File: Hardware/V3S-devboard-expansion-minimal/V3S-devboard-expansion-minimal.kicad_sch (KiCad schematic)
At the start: 2 parts, among them CN1 AS0BC21-S30BE-7H, CN2 AS0BC21-S30BE-7H

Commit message: expansion board work
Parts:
- added C1, C2: 100n, Capacitor_SMD:C_0603_1608Metric, symbol Device:C_Small
- added C10, C3, C5, C7, C8, C9: 10u, Capacitor_SMD:C_0603_1608Metric, symbol Device:C_Small
- added C4, C6: 1u, Capacitor_SMD:C_0603_1608Metric, symbol Device:C_Small
- added FPC1: AFC07-S50ECA-00, v3s-devboard-expansion-minimal:FPC-SMD_AFC07-S50ECA-00, symbol v3s-devboard-expansion-minimal:AFC07-S50ECA-00
- added J1, J2, J3: Conn_01x05_Pin, Connector_PinHeader_2.54mm:PinHeader_1x05_P2.54mm_Vertical, symbol Connector:Conn_01x05_Pin
- added J10: USB_C_Receptacle_USB2.0, Connector_USB:USB_C_Receptacle_HCTL_HC-TYPE-C-16P-01A, symbol Connector:USB_C_Receptacle_USB2.0
- added J11, J12, J4, J6: Conn_01x02_Pin, Connector_PinHeader_2.54mm:PinHeader_1x02_P2.54mm_Vertical, symbol Connector:Conn_01x02_Pin
- added J13: Conn_01x03_Pin, Connector_PinSocket_2.54mm:PinSocket_1x03_P2.54mm_Vertical, symbol Connector:Conn_01x03_Pin
- added J5: Conn_02x05_Odd_Even, Connector_PinHeader_2.54mm:PinHeader_2x05_P2.54mm_Vertical, symbol Connector_Generic:Conn_02x05_Odd_Even
- added J7: Conn_02x12_Odd_Even, Connector_PinSocket_2.54mm:PinSocket_2x12_P2.54mm_Vertical, symbol Connector_Generic:Conn_02x12_Odd_Even
- added J8: RJ45_Hanrun_HR911105A_Horizontal, Connector_RJ:RJ45_Hanrun_HR911105A_Horizontal, symbol Connector:RJ45_Hanrun_HR911105A_Horizontal
- added J9: Conn_02x03_Odd_Even, Connector_PinSocket_2.54mm:PinSocket_2x03_P2.54mm_Vertical, symbol Connector_Generic:Conn_02x03_Odd_Even
- added L1: 2.2u, Inductor_SMD:L_1008_2520Metric, symbol Device:L_Small
- added R1, R2, R3, R4: 100, Resistor_SMD:R_0603_1608Metric, symbol Device:R_Small_US
- added R10, R11, R8, R9: 51, Resistor_SMD:R_0603_1608Metric, symbol Device:R_Small_US
- added R12, R14: 5.1K, Resistor_SMD:R_0603_1608Metric, symbol Device:R_Small_US
- added R13: 4.7K, Resistor_SMD:R_0603_1608Metric, symbol Device:R_Small_US
- added R5, R7: 680, Resistor_SMD:R_0603_1608Metric, symbol Device:R_Small_US
- added R6: 10k, Resistor_SMD:R_0402_1005Metric, symbol Device:R_Small_US
- added U1: CP2102N-Axx-xQFN28, Package_DFN_QFN:QFN-28-1EP_5x5mm_P0.5mm_EP3.1x3.1mm, symbol Interface_USB:CP2102N-Axx-xQFN28
- added U2: XDFC-0522-50P, v3s-devboard-expansion-minimal:FPC-SMD_50P-P0.50_LX_XDFC-0522-50P, symbol v3s-devboard-expansion-minimal:XDFC-0522-50P
- added U3: AMS1117-3.3, Package_TO_SOT_SMD:SOT-223-3_TabPin2, symbol Regulator_Linear:AMS1117-3.3
- added U4: AMS1117-2.85, Package_TO_SOT_SMD:SOT-223-3_TabPin2, symbol Regulator_Linear:AMS1117-2.85
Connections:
- net 5V: now also J11.2 (Pin_2)
- net CSI.CSI_SCK: now also J7.9 (Pin_9)
- net CSI.CSI_SDA: now also J7.8 (Pin_8)
- net CSI.MCSI_CK_N: now also J7.2 (Pin_2)
- net CSI.MCSI_CK_P: now also J7.4 (Pin_4)
- net CSI.MCSI_D0_N: now also J7.5 (Pin_5)
- net CSI.MCSI_D0_P: now also J7.7 (Pin_7)
- net CSI.MCSI_D1_N: now also J7.1 (Pin_1)
- net CSI.MCSI_D1_P: now also J7.3 (Pin_3)
- net CSI.MCSI_MCLK: now also J7.6 (Pin_6)
- net ETH0.RX_N: now also J8.6 (RD-), R11.2
- net ETH0.RX_P: now also J8.3 (RD+), R10.2
- net ETH0.TX_N: now also J8.2 (TD-), R9.2
- net ETH0.TX_P: now also J8.1 (TD+), R8.2
- net ETH_LED_LINK: now also J8.10
- net ETH_LED_SPD: now also J8.11
- net GND: now also CN1.76, CN1.77, C1.1, C10.1, C2.1, C3.1, C4.1, C5.1, C6.1, C7.1, C8.1, C9.1, FPC1.43, FPC1.48, FPC1.49, FPC1.50, FPC1.51, FPC1.52, J10.A1 (GND), J10.A12 (GND), J10.B1 (GND), J10.B12 (GND), J10.S1 (SHIELD), J2.1 (Pin_1), J2.2 (Pin_2), J2.3 (Pin_3), J2.4 (Pin_4), J2.5 (Pin_5), J5.9 (Pin_9), J7.20 (Pin_20), J7.22 (Pin_22), J7.24 (Pin_24), J8.8, J8.SH, J9.5 (Pin_5), J9.6 (Pin_6), R1.2, R12.2, R14.2, R2.2, R3.2, R4.2, U1.29 (GND), U1.3 (GND), U2.43, U2.48, U2.49, U2.50, U2.51, U2.52, U3.1 (GND), U4.1 (GND)
- net LCD0.CLK: now also FPC1.13, U2.13
- net LCD0.DE: now also J6.1 (Pin_1)
- net LCD0.HSYNC: now also FPC1.12, U2.12
- net LCD0.VSYNC: now also FPC1.11, U2.11
- net LCD_D10: now also FPC1.26, U2.26
- net LCD_D11: now also FPC1.25, U2.25
- net LCD_D12: now also FPC1.24, U2.24
- net LCD_D13: now also FPC1.23, U2.23
- net LCD_D14: now also FPC1.22, U2.22
- net LCD_D15: now also FPC1.21, U2.21
- net LCD_D18: now also FPC1.20, U2.20
- net LCD_D19: now also FPC1.19, U2.19
- net LCD_D2: now also FPC1.32, U2.32
- net LCD_D20: now also FPC1.18, U2.18
- net LCD_D21: now also FPC1.17, U2.17
- net LCD_D22: now also FPC1.16, U2.16
- net LCD_D23: now also FPC1.15, U2.15
- net LCD_D3: now also FPC1.31, U2.31
- net LCD_D4: now also FPC1.30, U2.30
- net LCD_D5: now also FPC1.29, U2.29
- net LCD_D6: now also FPC1.28, U2.28
- net LCD_D7: now also FPC1.27, U2.27
- net PB4_PWM0: now also J7.16 (Pin_16)
- net PB5_PWM1: now also J7.15 (Pin_15)
- net PB6_SCK: now also J7.13 (Pin_13)
- net PB7_SDA: now also J7.14 (Pin_14)
- net SDC1.CLK: now also J7.10 (Pin_10)
- net SDC1.D0: now also J7.12 (Pin_12)
- net SDC1.D2: now also J7.11 (Pin_11)
- net UART0.RX: now also J9.1 (Pin_1)
- net UART0.TX: now also J9.2 (Pin_2)
- net UART2.CTS: now also J7.17 (Pin_17)
- net UART2.RX: now also J9.3 (Pin_3)
- net UART2.TX: now also J9.4 (Pin_4)
- net USB.USB_ID: now also J7.18 (Pin_18)
- new net: C1.2, J8.5 (RCT), R10.1, R11.1
- new net: C2.2, J8.4 (TCT), L1.2, R8.1, R9.1
- new net: FPC1.44, U2.44
- new net: FPC1.45, U2.45
- new net: FPC1.46, U2.46
- new net: FPC1.47, U2.47
- new net: J8.9, R7.1
- new net: J10.B5 (CC2), R14.1
- new net: J8.12, R5.1
- new net: R13.1, U1.9 (~{RST})
- new net: J10.A5 (CC1), R12.1
- new net: J12.1 (Pin_1), U1.25 (RXD)
- new net: J12.2 (Pin_2), U1.26 (TXD)
- new net 2V85: C7.2, J13.1 (Pin_1), U4.2 (VO)
- new net 3V3: C5.2, C6.2, C8.2, J13.3 (Pin_3), J7.19 (Pin_19), J7.21 (Pin_21), J7.23 (Pin_23), L1.1, R13.2, R5.2, R7.2, U1.6 (VDD), U1.7 (VREGIN), U3.2 (VO)
- new net IM0: FPC1.6, J1.1 (Pin_1), U2.6
- new net IM1: FPC1.7, J1.2 (Pin_2), U2.7
- new net IM2: FPC1.8, J1.3 (Pin_3), U2.8
- new net IM3: FPC1.9, J1.4 (Pin_4), U2.9
- new net LCD_CS: FPC1.38, J5.7 (Pin_7), U2.38
- new net LCD_DE: FPC1.14, J6.2 (Pin_2), U2.14
- new net LCD_DRX: FPC1.36, J5.4 (Pin_4), U2.36
- new net LCD_RD: FPC1.35, J5.2 (Pin_2), U2.35
- new net LCD_RST: FPC1.10, J1.5 (Pin_5), R6.2, U2.10
- new net LCD_SCL: FPC1.37, J5.5 (Pin_5), U2.37
- new net LCD_SDI: FPC1.34, J5.3 (Pin_3), U2.34
- new net LCD_SDO: FPC1.33, J5.1 (Pin_1), U2.33
- new net LCD_TE: FPC1.39, J5.6 (Pin_6), U2.39
- new net LCD_VDD: FPC1.40, FPC1.41, FPC1.42, U2.40, U2.41, U2.42
- new net LEDA: FPC1.1, J4.2 (Pin_2), U2.1
- new net LEDK1: FPC1.2, R1.1, U2.2
- new net LEDK2: FPC1.3, R2.1, U2.3
- new net LEDK3: FPC1.4, R3.1, U2.4
- new net LEDK4: FPC1.5, R4.1, U2.5
- new net LED_VDD: J13.2 (Pin_2), J3.1 (Pin_1), J3.2 (Pin_2), J3.3 (Pin_3), J3.4 (Pin_4), J3.5 (Pin_5), J4.1 (Pin_1), R6.1
- new net USB_D_N: J10.A7 (D-), J10.B7 (D-), U1.5 (D-)
- new net USB_D_P: J10.A6 (D+), J10.B6 (D+), U1.4 (D+)
- new net VBUS_IN: C10.2, C3.2, C4.2, C9.2, J10.A4 (VBUS), J10.A9 (VBUS), J10.B4 (VBUS), J10.B9 (VBUS), J11.1 (Pin_1), U1.8 (VBUS), U3.3 (VI), U4.3 (VI)
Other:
- note added: "red 23-18 green 15-10 blue 2-7"
- note added: "top: C262650 bottom: C262574 clam both: C7527533"
- moved on the sheet: CN1, CN2

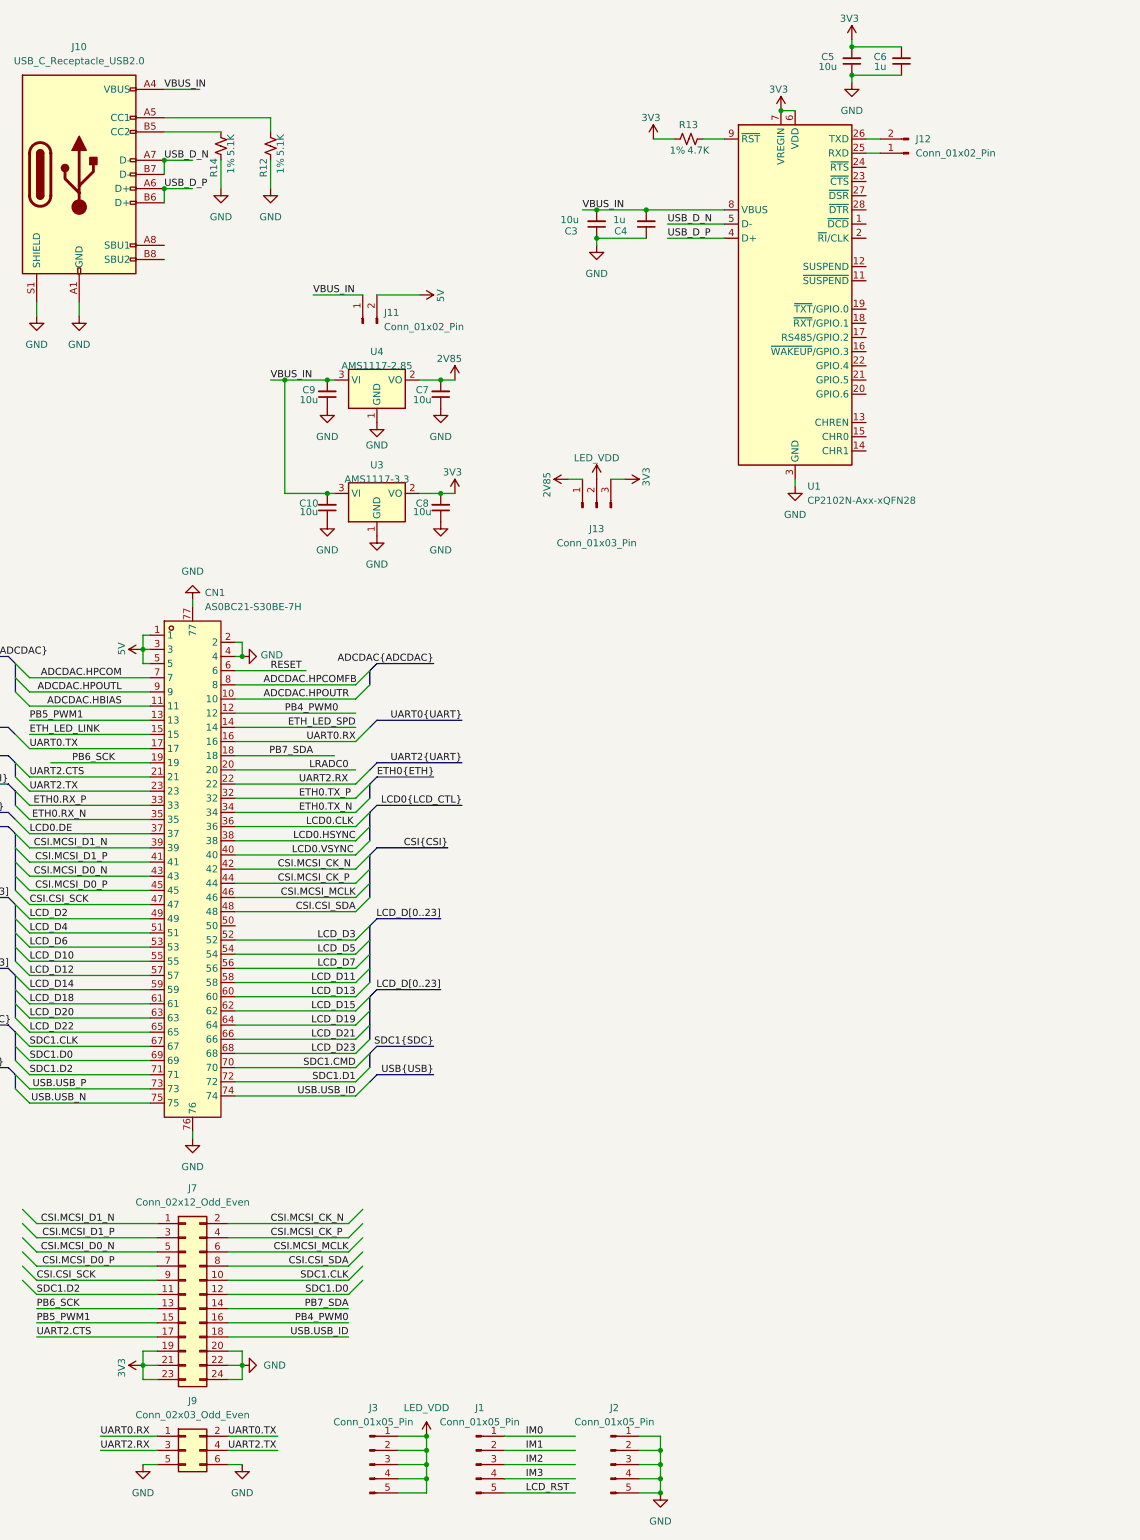
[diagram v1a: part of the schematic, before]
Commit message: expansion layout and schematic
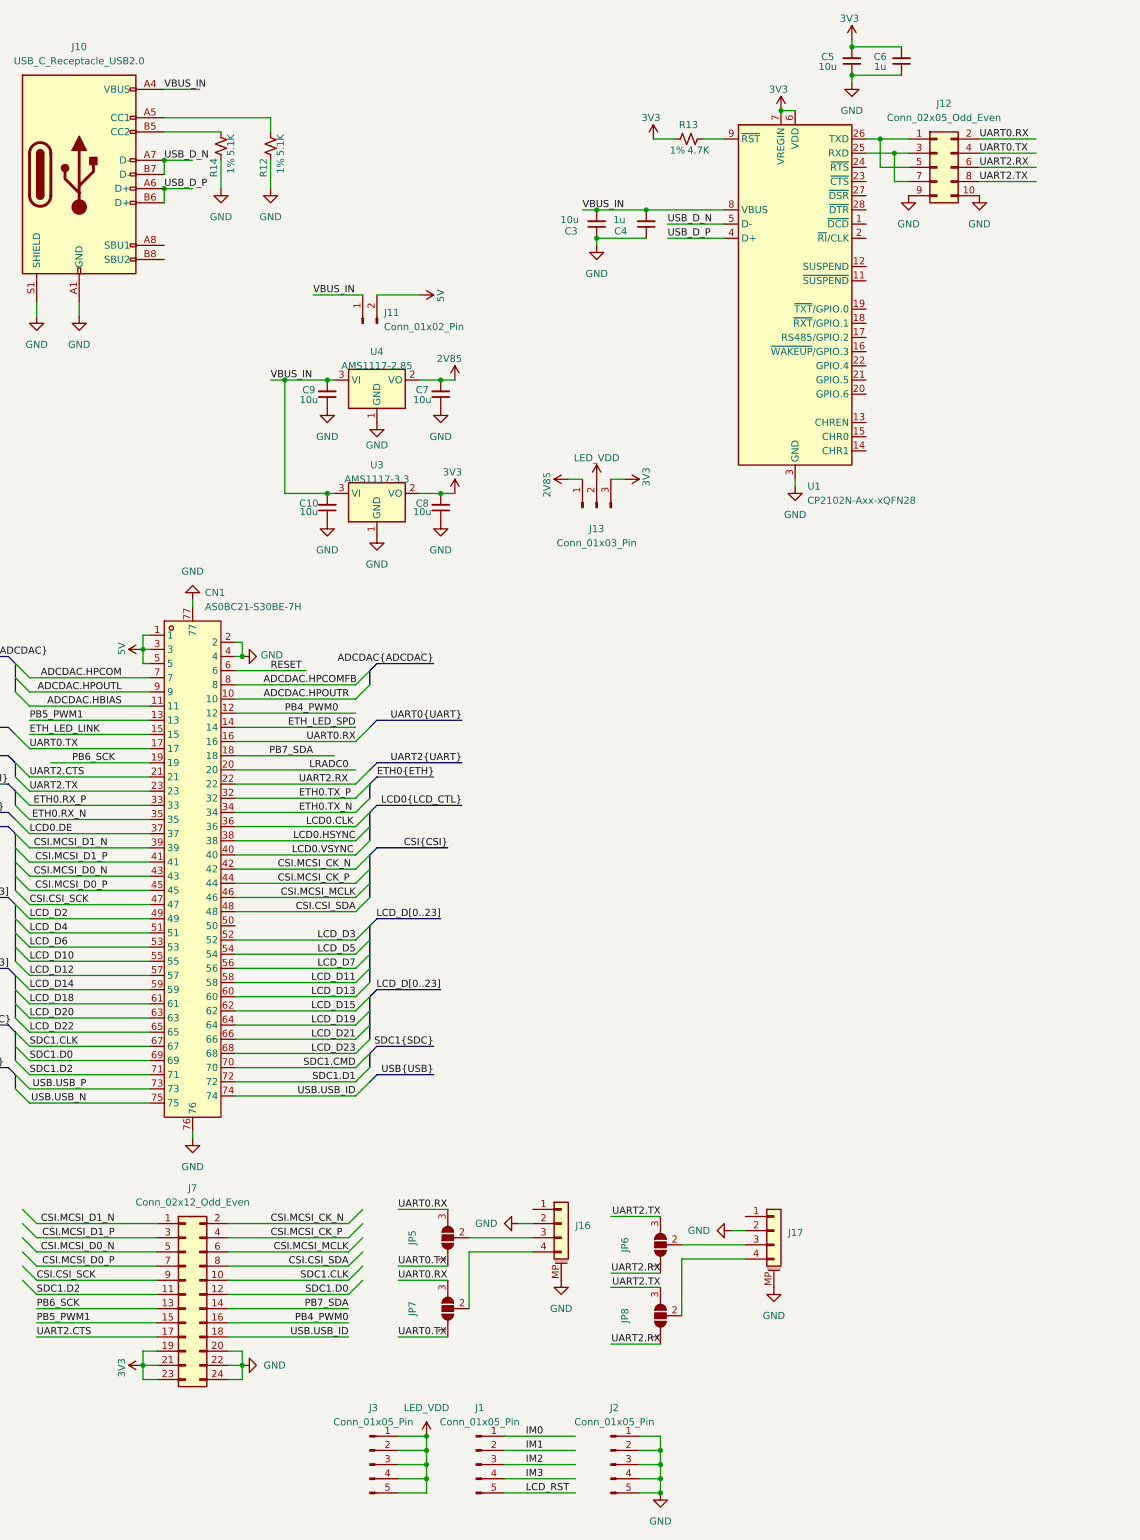
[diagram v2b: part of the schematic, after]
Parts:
- removed J12: Conn_01x02_Pin, Connector_PinHeader_2.54mm:PinHeader_1x02_P2.54mm_Vertical, symbol Connector:Conn_01x02_Pin
- removed J9: Conn_02x03_Odd_Even, Connector_PinSocket_2.54mm:PinSocket_2x03_P2.54mm_Vertical, symbol Connector_Generic:Conn_02x03_Odd_Even
- added J12: Conn_02x05_Odd_Even, Connector_PinHeader_2.54mm:PinHeader_2x05_P2.54mm_Vertical, symbol Connector_Generic:Conn_02x05_Odd_Even
- added J16, J17: Conn_01x04_MountingPin, v3s-devboard-expansion-minimal:CONN-SMD_HCZZ0021-4, symbol Connector_Generic_MountingPin:Conn_01x04_MountingPin
- added JP5, JP6, JP7, JP8: SolderJumper_3_Open, Jumper:SolderJumper-3_P1.3mm_Open_RoundedPad1.0x1.5mm_NumberLabels, symbol Jumper:SolderJumper_3_Open
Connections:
- net GND: now also J12.10 (Pin_10), J12.9 (Pin_9), J16.2 (Pin_2), J16.MP (MountPin), J17.2 (Pin_2), J17.MP (MountPin)
- net UART0.RX: now also J12.2 (Pin_2), JP5.3 (B), JP7.3 (B)
- net UART0.TX: now also J12.4 (Pin_4), JP5.1 (A), JP7.1 (A)
- net UART2.RX: now also J12.6 (Pin_6), JP6.1 (A), JP8.1 (A)
- net UART2.TX: now also J12.8 (Pin_8), JP6.3 (B), JP8.3 (B)
- net at U1.25 (RXD): now also J12.3 (Pin_3), J12.7 (Pin_7)
- net at U1.26 (TXD): now also J12.1 (Pin_1), J12.5 (Pin_5)
- new net: J16.4 (Pin_4), JP7.2 (C)
- new net: J17.3 (Pin_3), JP6.2 (C)
- new net: J17.4 (Pin_4), JP8.2 (C)
- new net: J16.3 (Pin_3), JP5.2 (C)

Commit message: working on final touches
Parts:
- added H1: MountingHole_Pad, v3s-devboard-expansion-minimal:screwnut, symbol Mechanical:MountingHole_Pad
- added R15: 8.2K, Resistor_SMD:R_0603_1608Metric, symbol Device:R_Small_US
- added R16: 10K, Resistor_SMD:R_0603_1608Metric, symbol Device:R_Small_US
- added R17: 11K, Resistor_SMD:R_0603_1608Metric, symbol Device:R_Small_US
- added R18: 6.8K, Resistor_SMD:R_0603_1608Metric, symbol Device:R_Small_US
- added SW1, SW2, SW3, SW4, SW5: SW_MEC_5E, v3s-devboard-module:SW_SKRPACE010, symbol Switch:SW_MEC_5E
- J12: footprint Connector_PinHeader_2.54mm:PinHeader_2x05_P2.54mm_Vertical -> Connector_PinHeader_2.54mm:PinHeader_2x05_P2.54mm_Vertical_SMD
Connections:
- net LED_VDD is gone; now on net LCD_VDD: J13.2 (Pin_2), J3.1 (Pin_1), J3.2 (Pin_2), J3.3 (Pin_3), J3.4 (Pin_4), J3.5 (Pin_5), J4.1 (Pin_1), R6.1
- net 3V3: now also J7.20 (Pin_20), J7.22 (Pin_22), J7.24 (Pin_24); no longer J7.19 (Pin_19), J7.21 (Pin_21), J7.23 (Pin_23)
- net GND: now also J7.19 (Pin_19), J7.21 (Pin_21), J7.23 (Pin_23), H1.1, SW1.1, SW1.2, SW2.2, SW3.2, SW4.2, SW5.2; no longer J7.20 (Pin_20), J7.22 (Pin_22), J7.24 (Pin_24)
- net LRADC0: now also R18.1
- net RESET: now also SW1.3 (K), SW1.4 (A)
- new net: R16.2, R17.1, SW4.3 (K)
- new net: R15.1, R18.2, SW2.3 (K)
- new net: R15.2, R16.1, SW3.3 (K)
- new net: R17.2, SW5.3 (K)

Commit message: Minor changes. Sent to fab
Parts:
- C5, C6, J1, J11, J12, J13, J2, J3, J4, J5, J6, R1, R2, R3, R4, R6: now left out of the parts list
- H1: LCSC (none) -> C2928188
- J10: LCSC (none) -> C2894897
- J7: LCSC (none) -> C2685134
- R15: LCSC C60491 -> C25981
- R16: LCSC C60491 -> C25804
- R17: LCSC C60491 -> C103227
- R18: LCSC C60491 -> C23212
- SW1, SW2, SW3, SW4, SW5: LCSC (none) -> C139797
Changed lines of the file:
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@@
 		(unit 1)
 		(exclude_from_sim no)
-		(in_bom yes)
+		(in_bom no)
 		(on_board yes)
 		(dnp no)
@@
 			)
 		)
+		(property "LCSC" "C139797"
+			(at 147.32 173.99 90)
+			(effects
+				(font
+					(size 1.27 1.27)
+				)
+				(hide yes)
+			)
+		)
 		(pin "1"
 		)
@@
 		(unit 1)
 		(exclude_from_sim no)
-		(in_bom yes)
+		(in_bom no)
 		(on_board yes)
 		(dnp no)
@@
 			)
 		)
+		(property "LCSC" "C139797"
+			(at 220.98 175.26 90)
+			(effects
+				(font
+					(size 1.27 1.27)
+				)
+				(hide yes)
+			)
+		)
 		(pin "1"
 		)
@@
 			)
 		)
-		(property "LCSC" "C60491"
+		(property "LCSC" "C25981"
 			(at 203.2 165.1 90)
 			(effects
@@
 			)
 		)
+		(property "LCSC" "C139797"
+			(at 199.39 175.26 90)
+			(effects
+				(font
+					(size 1.27 1.27)
+				)
+				(hide yes)
+			)
+		)
 		(pin "1"
 		)
@@
 		(unit 1)
 		(exclude_from_sim no)
-		(in_bom yes)
+		(in_bom no)
 		(on_board yes)
 		(dnp no)
@@
 		(unit 1)
 		(exclude_from_sim no)
-		(in_bom yes)
+		(in_bom no)
 		(on_board yes)
 		(dnp no)
@@
 			)
 		)
+		(property "LCSC" "C2928188"
+			(at 274.32 140.97 0)
+			(effects
+				(font
+					(size 1.27 1.27)
+				)
+				(hide yes)
+			)
+		)
 		(pin "1"
 		)
@@
 		(unit 1)
 		(exclude_from_sim no)
-		(in_bom yes)
+		(in_bom no)
 		(on_board yes)
 		(dnp no)
@@
 		(unit 1)
 		(exclude_from_sim no)
-		(in_bom yes)
+		(in_bom no)
 		(on_board yes)
 		(dnp no)
@@
 		(unit 1)
 		(exclude_from_sim no)
-		(in_bom yes)
+		(in_bom no)
 		(on_board yes)
 		(dnp no)
@@
 		(unit 1)
 		(exclude_from_sim no)
-		(in_bom yes)
+		(in_bom no)
 		(on_board yes)
 		(dnp no)
@@
 		(unit 1)
 		(exclude_from_sim no)
-		(in_bom yes)
+		(in_bom no)
 		(on_board yes)
 		(dnp no)
@@
 			)
 		)
+		(property "LCSC" "C2894897"
+			(at 50.8 41.91 0)
+			(effects
+				(font
+					(size 1.27 1.27)
+				)
+				(hide yes)
+			)
+		)
 		(pin "A1"
 		)
@@
 			)
 		)
-		(property "LCSC" "C60491"
+		(property "LCSC" "C23212"
 			(at 191.77 165.1 90)
 			(effects
@@
 			)
 		)
-		(property "LCSC" "C60491"
+		(property "LCSC" "C25804"
 			(at 214.63 165.1 90)
 			(effects
@@
 		(unit 1)
 		(exclude_from_sim no)
-		(in_bom yes)
+		(in_bom no)
 		(on_board yes)
 		(dnp no)
@@
 			)
 		)
+		(property "LCSC" "C2685134"
+			(at 69.85 242.57 0)
+			(effects
+				(font
+					(size 1.27 1.27)
+				)
+				(hide yes)
+			)
+		)
 		(pin "21"
 		)
@@
 		(unit 1)
 		(exclude_from_sim no)
-		(in_bom yes)
+		(in_bom no)
 		(on_board yes)
 		(dnp no)
@@
 			)
 		)
-		(property "LCSC" "C60491"
+		(property "LCSC" "C103227"
 			(at 224.79 165.1 90)
 			(effects
@@
 			)
 		)
+		(property "LCSC" "C139797"
+			(at 210.82 175.26 90)
+			(effects
+				(font
+					(size 1.27 1.27)
+				)
+				(hide yes)
+			)
+		)
 		(pin "1"
 		)
@@
 		(unit 1)
 		(exclude_from_sim no)
-		(in_bom yes)
+		(in_bom no)
 		(on_board yes)
 		(dnp no)
@@
 		(unit 1)
 		(exclude_from_sim no)
-		(in_bom yes)
+		(in_bom no)
 		(on_board yes)
 		(dnp no)
@@
 		(unit 1)
 		(exclude_from_sim no)
-		(in_bom yes)
+		(in_bom no)
 		(on_board yes)
 		(dnp no)
@@
 		(unit 1)
 		(exclude_from_sim no)
-		(in_bom yes)
+		(in_bom no)
 		(on_board yes)
 		(dnp no)
@@
 			)
 		)
+		(property "LCSC" "C139797"
+			(at 231.14 175.26 90)
+			(effects
+				(font
+					(size 1.27 1.27)
+				)
+				(hide yes)
+			)
+		)
 		(pin "1"
 		)
@@
 		(unit 1)
 		(exclude_from_sim no)
-		(in_bom yes)
+		(in_bom no)
 		(on_board yes)
 		(dnp no)
